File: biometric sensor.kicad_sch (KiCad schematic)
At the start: 1 part, among them U1 MAX30102

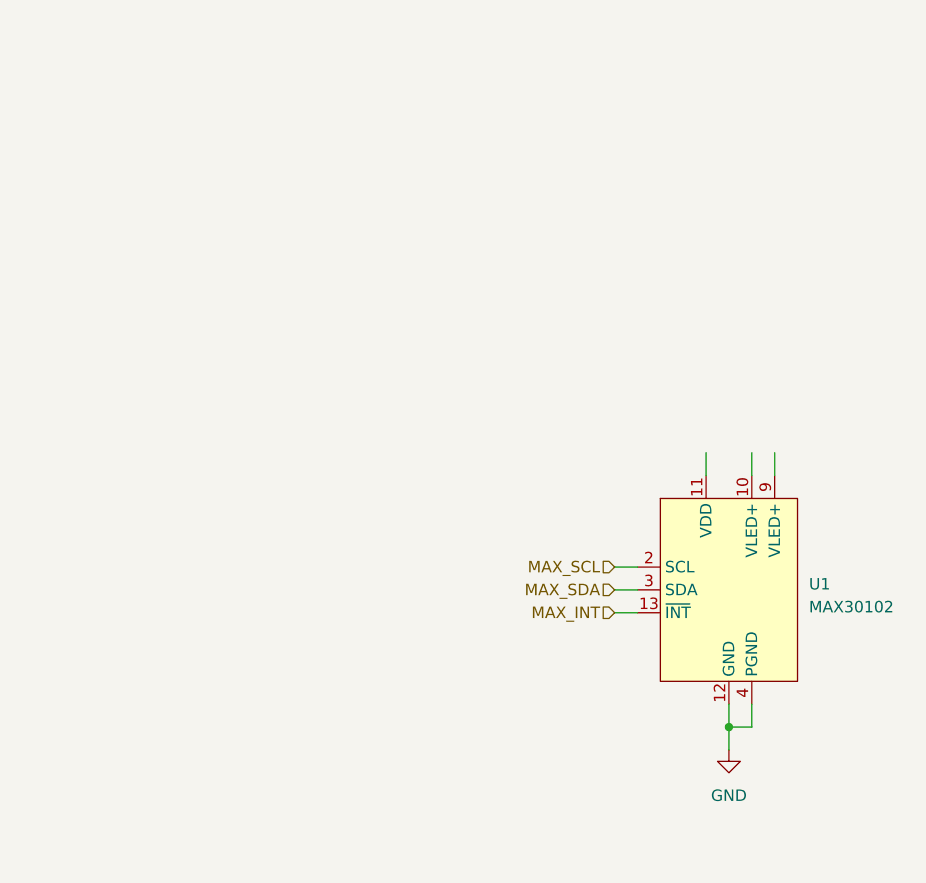
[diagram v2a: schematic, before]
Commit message: added decoupling capacitors to sensors
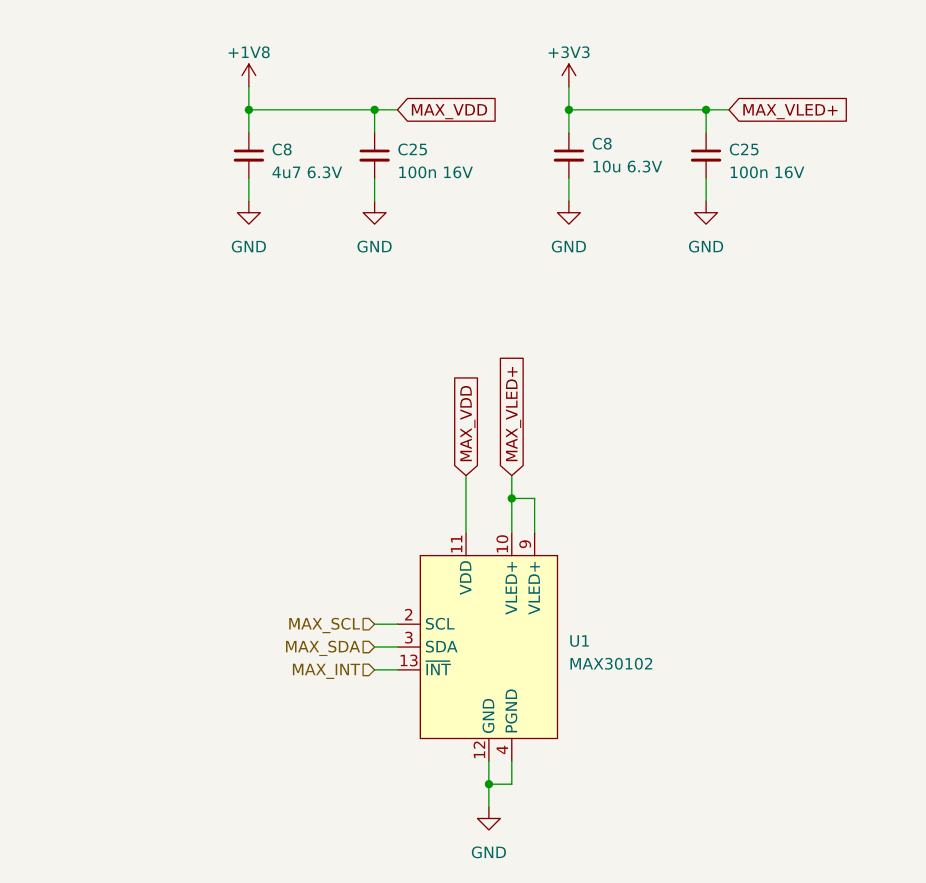
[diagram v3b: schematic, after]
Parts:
- added C25 (x2): 100n 16V, Capacitor_SMD:C_0402_1005Metric, symbol Device:C_Small
- added C8: 4u7 6.3V, Capacitor_SMD:C_0402_1005Metric, symbol Device:C_Small
- added C8: 10u 6.3V, Capacitor_SMD:C_0402_1005Metric, symbol Device:C_Small
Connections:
- net GND: now also C25.2, C25.2, C8.2, C8.2
- net +3V3: now reaches U1.10 (VLED+)
- net +3V3: now also U1.9 (VLED+), C25.1, C8.1
- net +1V8: now reaches U1.11 (VDD)
- net +1V8: now also C25.1, C8.1
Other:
- moved on the sheet: U1

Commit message: cleaned up supply labels
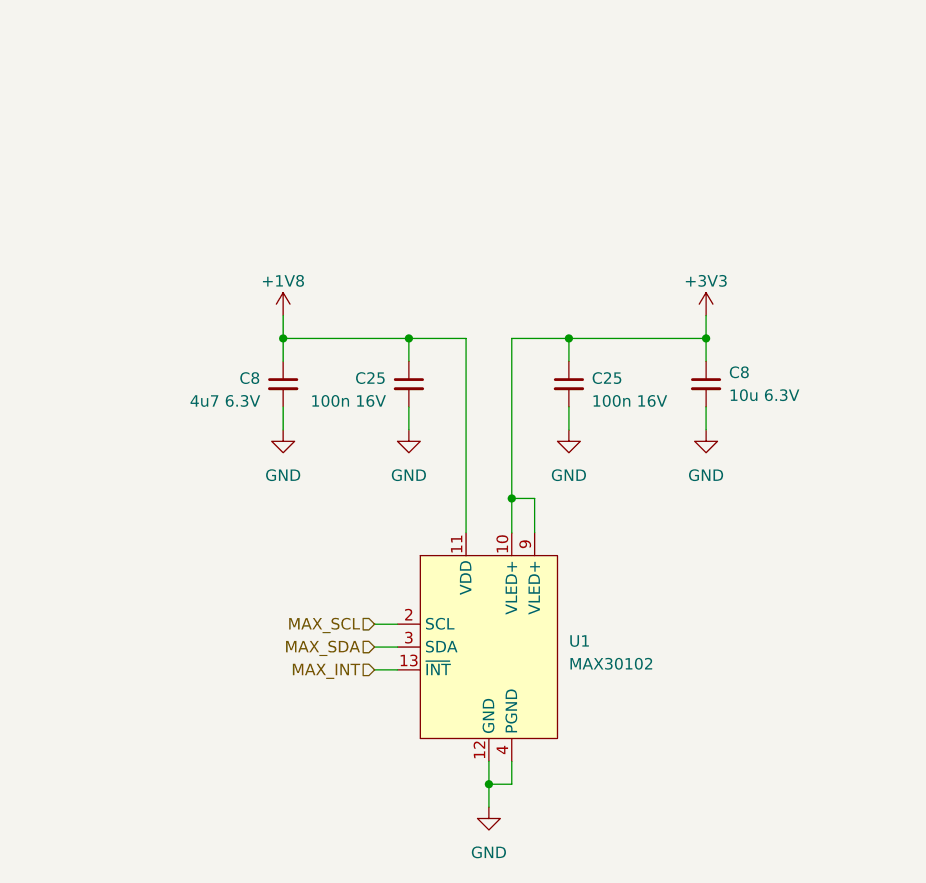
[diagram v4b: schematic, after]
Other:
- moved on the sheet: C25, C8

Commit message: added ambient light_sensor.kicad_sch
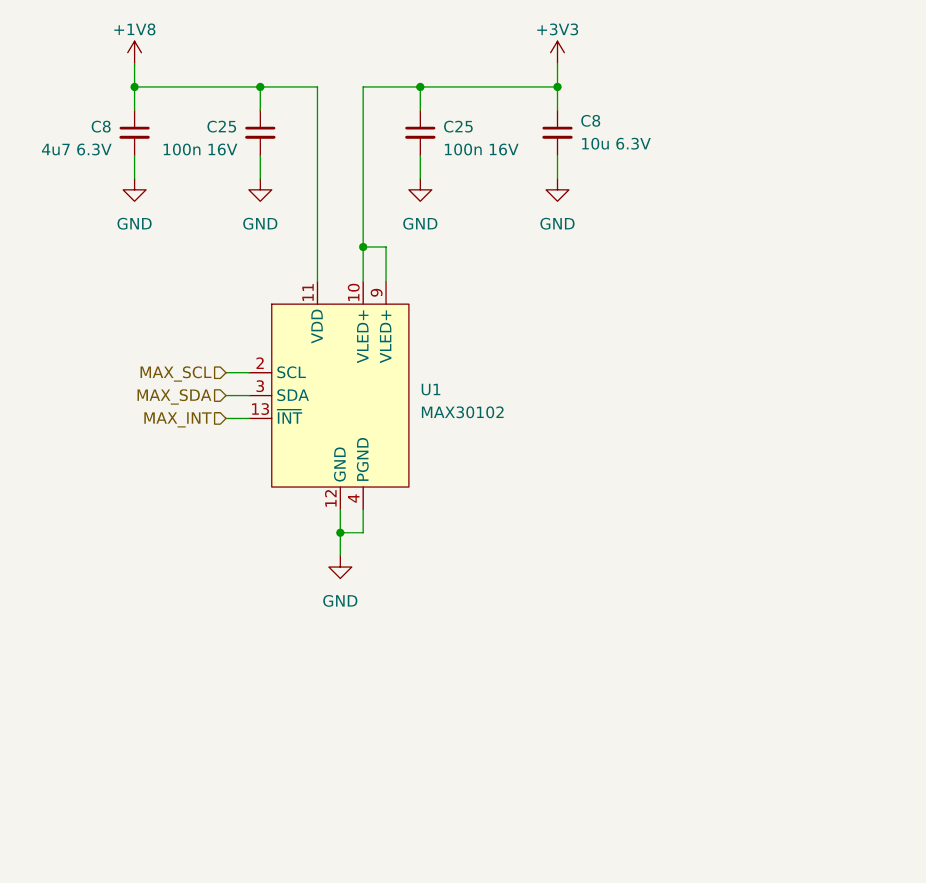
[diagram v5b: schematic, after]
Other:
- moved on the sheet: C25, C8, U1

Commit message: cleaned up symbol fields table and removed unused or duplicate fields.
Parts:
- U1: FootprintDatasheet https://pdfserv.maximintegrated.com/land_patterns/90-0602.P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 -> (none)
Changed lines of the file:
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@@
         )
         (path "/017c50c6-333c-4d31-ad5a-278994a09b14/db6ac415-a2f9-4935-934d-f0e91f8b44d3"
-          (reference "#PWR043") (unit 1)
+          (reference "#PWR064") (unit 1)
         )
       )
@@
         )
         (path "/017c50c6-333c-4d31-ad5a-278994a09b14/db6ac415-a2f9-4935-934d-f0e91f8b44d3"
-          (reference "C17") (unit 1)
+          (reference "C24") (unit 1)
         )
       )
@@
         )
         (path "/017c50c6-333c-4d31-ad5a-278994a09b14/db6ac415-a2f9-4935-934d-f0e91f8b44d3"
-          (reference "#PWR070") (unit 1)
+          (reference "#PWR060") (unit 1)
         )
       )
@@
         )
         (path "/017c50c6-333c-4d31-ad5a-278994a09b14/db6ac415-a2f9-4935-934d-f0e91f8b44d3"
-          (reference "C11") (unit 1)
+          (reference "C27") (unit 1)
         )
       )
@@
         )
         (path "/017c50c6-333c-4d31-ad5a-278994a09b14/db6ac415-a2f9-4935-934d-f0e91f8b44d3"
-          (reference "#PWR040") (unit 1)
+          (reference "#PWR059") (unit 1)
         )
       )
@@
         )
         (path "/017c50c6-333c-4d31-ad5a-278994a09b14/db6ac415-a2f9-4935-934d-f0e91f8b44d3"
-          (reference "#PWR038") (unit 1)
+          (reference "#PWR063") (unit 1)
         )
       )
@@
         )
         (path "/017c50c6-333c-4d31-ad5a-278994a09b14/db6ac415-a2f9-4935-934d-f0e91f8b44d3"
-          (reference "C12") (unit 1)
+          (reference "C26") (unit 1)
         )
       )
@@
     )
     (property "Datasheet" "https://www.mouser.de/datasheet/2/609/MAX30102-3128143.pdf" (at 135.89 62.23 0)
-      (effects (font (size 1.27 1.27)) hide)
-    )
-    (property "FootprintDatasheet" "https://pdfserv.maximintegrated.com/land_patterns/90-0602.PDF" (at 135.89 64.77 0)
       (effects (font (size 1.27 1.27)) hide)
     )
@@
         )
         (path "/017c50c6-333c-4d31-ad5a-278994a09b14/db6ac415-a2f9-4935-934d-f0e91f8b44d3"
-          (reference "#PWR069") (unit 1)
+          (reference "#PWR058") (unit 1)
         )
       )
@@
         )
         (path "/017c50c6-333c-4d31-ad5a-278994a09b14/db6ac415-a2f9-4935-934d-f0e91f8b44d3"
-          (reference "C31") (unit 1)
+          (reference "C25") (unit 1)
         )
       )
@@
         )
         (path "/017c50c6-333c-4d31-ad5a-278994a09b14/db6ac415-a2f9-4935-934d-f0e91f8b44d3"
-          (reference "#PWR071") (unit 1)
+          (reference "#PWR061") (unit 1)
         )
       )
@@
         )
         (path "/017c50c6-333c-4d31-ad5a-278994a09b14/db6ac415-a2f9-4935-934d-f0e91f8b44d3"
-          (reference "#PWR039") (unit 1)
-        )
-      )
+          (reference "#PWR062") (unit 1)
+        )
+      )

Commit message: Fix unconnected nets
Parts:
- U1: FootprintDatasheet (none) -> https://pdfserv.maximintegrated.com/land_patterns/90-0602.P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
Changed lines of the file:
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@@
+      (effects (font (size 1.27 1.27)) hide)
+    )
+    (property "FootprintDatasheet" "https://pdfserv.maximintegrated.com/land_patterns/90-0602.PDF" (at 135.89 64.77 0)
       (effects (font (size 1.27 1.27)) hide)
     )

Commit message: added missing MFN numbers
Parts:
- C25: sourced (none) -> y
- C8: MFN 187-CL05A475KQ5NRNC -> 187-CL05A475KQ5NRNC; sourced (none) -> y
- C8: MFN 81-GRM155R60J106M05D -> 81-GRM155R60J106M05D; sourced (none) -> y
- U1: MFN (none) -> 700-MAX30102EFD+T; sourced (none) -> y
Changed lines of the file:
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@@
       (effects (font (size 1.27 1.27)) hide)
     )
-    (property "MFN" " 187-CL05A475KQ5NRNC " (at 73.66 40.64 0)
+    (property "MFN" "187-CL05A475KQ5NRNC " (at 73.66 40.64 0)
+      (effects (font (size 1.27 1.27)) hide)
+    )
+    (property "sourced" "y" (at 73.66 40.64 0)
       (effects (font (size 1.27 1.27)) hide)
     )
@@
       (effects (font (size 1.27 1.27)) hide)
     )
-    (property "MFN" " 81-GRM155R60J106M05D " (at 120.65 40.64 0)
+    (property "MFN" "81-GRM155R60J106M05D " (at 120.65 40.64 0)
+      (effects (font (size 1.27 1.27)) hide)
+    )
+    (property "sourced" "y" (at 120.65 40.64 0)
       (effects (font (size 1.27 1.27)) hide)
     )
@@
       (effects (font (size 1.27 1.27)) hide)
     )
+    (property "sourced" "y" (at 105.41 40.64 0)
+      (effects (font (size 1.27 1.27)) hide)
+    )
     (pin "1")
     (pin "2")
@@
     )
     (property "FootprintDatasheet" "https://pdfserv.maximintegrated.com/land_patterns/90-0602.PDF" (at 135.89 64.77 0)
+      (effects (font (size 1.27 1.27)) hide)
+    )
+    (property "MFN" "700-MAX30102EFD+T " (at 96.52 67.31 0)
+      (effects (font (size 1.27 1.27)) hide)
+    )
+    (property "sourced" "y" (at 96.52 67.31 0)
       (effects (font (size 1.27 1.27)) hide)
     )
@@
       (effects (font (size 1.27 1.27)) hide)
     )
+    (property "sourced" "y" (at 87.63 40.64 0)
+      (effects (font (size 1.27 1.27)) hide)
+    )
